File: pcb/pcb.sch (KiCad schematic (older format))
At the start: 21 parts

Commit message: 1n4148->1n4004 and connector changes
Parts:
- removed D? (x2): 1N4148, Diode_THT:D_DO-35_SOD27_P7.62mm_Horizontal, symbol Device:D_Small
- removed J?: Screw_Terminal_01x03, symbol Connector:Screw_Terminal_01x03
- added D? (x2): 1N4004, Diode_THT:D_DO-41_SOD81_P10.16mm_Horizontal, symbol Device:D_Small
- added J?: JST XH-3P, symbol Connector:Conn_01x03_Male
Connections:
- net +3V3: now also D?.2 (A)
- net GND: now also J?.3 (Pin_3)
- net UNLOCK_PIN: now also J?.2 (Pin_2)
- net VBUS: now also D?.1 (K), J?.1 (Pin_1)
- net at FH?.1: now also D?.2 (A)
- net at J?.1 (Pin_1), J?.2 (Pin_2), J?.3 (Pin_3)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: now also D?.1 (K)
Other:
- moved on the sheet: D?, FH?, J?
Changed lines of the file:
@@
 $EndComp
 $Comp
-L Connector:Screw_Terminal_01x03 J?
-U 1 1 6273A423
-P 8250 4700
-F 0 "J?" H 8168 4467 50  0000 C CNN
-F 1 "Screw_Terminal_01x03" H 8168 4466 50  0001 C CNN
-F 2 "" H 8250 4700 50  0001 C CNN
-F 3 "~" H 8250 4700 50  0001 C CNN
-	1    8250 4700
-	-1   0    0    1
-$EndComp
-$Comp
 L power:GND #PWR?
 U 1 1 6273AC33
@@
 L Connector:Screw_Terminal_01x02 J?
 U 1 1 627917BC
-P 8150 2900
-F 0 "J?" H 8230 2846 50  0000 L CNN
-F 1 "Screw_Terminal_01x02" H 8230 2801 50  0001 L CNN
-F 2 "" H 8150 2900 50  0001 C CNN
-F 3 "~" H 8150 2900 50  0001 C CNN
-	1    8150 2900
+P 8150 3000
+F 0 "J?" H 8230 2946 50  0000 L CNN
+F 1 "Screw_Terminal_01x02" H 8230 2901 50  0001 L CNN
+F 2 "" H 8150 3000 50  0001 C CNN
+F 3 "~" H 8150 3000 50  0001 C CNN
+	1    8150 3000
 	1    0    0    -1
 $EndComp
 Wire Wire Line
-	7900 3000 7950 3000
+	7900 3100 7950 3100
 Wire Wire Line
-	7900 2900 7950 2900
+	7900 3000 7950 3000
 $Comp
 L power:GND #PWR?
 U 1 1 627949F4
-P 7900 3200
-F 0 "#PWR?" H 7900 2950 50  0001 C CNN
-F 1 "GND" H 7905 3027 50  0000 C CNN
-F 2 "" H 7900 3200 50  0001 C CNN
-F 3 "" H 7900 3200 50  0001 C CNN
-	1    7900 3200
+P 7900 3300
+F 0 "#PWR?" H 7900 3050 50  0001 C CNN
+F 1 "GND" H 7905 3127 50  0000 C CNN
+F 2 "" H 7900 3300 50  0001 C CNN
+F 3 "" H 7900 3300 50  0001 C CNN
+	1    7900 3300
 	1    0    0    -1
 $EndComp
@@
 	8500 5000 8500 4800
 Wire Wire Line
-	7150 3150 7150 3200
+	7150 3250 7150 3300
 $Comp
 L Device:D_Zener_Small D?
 U 1 1 628663B7
-P 7150 3050
-F 0 "D?" V 7104 3118 50  0000 L CNN
-F 1 "Vz=15" V 7195 3118 50  0000 L CNN
-F 2 "" V 7150 3050 50  0001 C CNN
-F 3 "~" V 7150 3050 50  0001 C CNN
-	1    7150 3050
+P 7150 3150
+F 0 "D?" V 7104 3218 50  0000 L CNN
+F 1 "Vz=15" V 7195 3218 50  0000 L CNN
+F 2 "" V 7150 3150 50  0001 C CNN
+F 3 "~" V 7150 3150 50  0001 C CNN
+	1    7150 3150
 	0    -1   1    0
 $EndComp
@@
 L power:VBUS #PWR?
 U 1 1 62777264
-P 7150 2850
-F 0 "#PWR?" H 7150 2700 50  0001 C CNN
-F 1 "VBUS" H 7165 3023 50  0000 C CNN
-F 2 "" H 7150 2850 50  0001 C CNN
-F 3 "" H 7150 2850 50  0001 C CNN
-	1    7150 2850
+P 7150 2950
+F 0 "#PWR?" H 7150 2800 50  0001 C CNN
+F 1 "VBUS" H 7165 3123 50  0000 C CNN
+F 2 "" H 7150 2950 50  0001 C CNN
+F 3 "" H 7150 2950 50  0001 C CNN
+	1    7150 2950
 	1    0    0    -1
 $EndComp
@@
 L power:GND #PWR?
 U 1 1 628C5A12
-P 7150 3200
-F 0 "#PWR?" H 7150 2950 50  0001 C CNN
-F 1 "GND" H 7155 3027 50  0000 C CNN
-F 2 "" H 7150 3200 50  0001 C CNN
-F 3 "" H 7150 3200 50  0001 C CNN
-	1    7150 3200
+P 7150 3300
+F 0 "#PWR?" H 7150 3050 50  0001 C CNN
+F 1 "GND" H 7155 3127 50  0000 C CNN
+F 2 "" H 7150 3300 50  0001 C CNN
+F 3 "" H 7150 3300 50  0001 C CNN
+	1    7150 3300
 	1    0    0    -1
 $EndComp
 Wire Wire Line
-	7900 3000 7900 3200
+	7900 3100 7900 3300
 $Comp
 L power:+3V3 #PWR?
@@
 Text Label 7650 5950 3    50   ~ 0
 GPIO_0
-$Comp
-L Device:D_Small D?
-U 1 1 629C5C10
-P 7400 2900
-F 0 "D?" H 7400 3105 50  0000 C CNN
-F 1 "1N4148" H 7400 3014 50  0000 C CNN
-F 2 "Diode_THT:D_DO-35_SOD27_P7.62mm_Horizontal" H 7400 2725 50  0001 C CNN
-F 3 "https://assets.nexperia.com/documents/data-sheet/1N4148_1N4448.pdf" H 7400 2900 50  0001 C CNN
-	1    7400 2900
-	1    0    0    -1
-$EndComp
 Wire Wire Line
-	7500 2900 7700 2900
+	7500 3000 7700 3000
 $Comp
 L Device:Fuse_Small FH?
 U 1 1 628BC0F0
-P 7800 2900
-F 0 "FH?" H 7800 3085 50  0000 C CNN
-F 1 "F5196-ND" H 7800 2994 50  0000 C CNN
-F 2 "project:Blade Fuse Holder" H 7800 2900 50  0001 C CNN
-F 3 "https://www.digikey.com/en/products/detail/littelfuse-inc/178-6164-0002/2515918?s=N4IgTCBcDaIGIFYCMBOAbAWgHIBEQF0BfIA" H 7800 2900 50  0001 C CNN
-	1    7800 2900
+P 7800 3000
+F 0 "FH?" H 7800 3185 50  0000 C CNN
+F 1 "F5196-ND" H 7800 3094 50  0000 C CNN
+F 2 "project:Blade Fuse Holder" H 7800 3000 50  0001 C CNN
+F 3 "https://www.digikey.com/en/products/detail/littelfuse-inc/178-6164-0002/2515918?s=N4IgTCBcDaIGIFYCMBOAbAWgHIBEQF0BfIA" H 7800 3000 50  0001 C CNN
+	1    7800 3000
 	1    0    0    -1
 $EndComp
 Wire Wire Line
-	7150 2850 7150 2900
+	7150 2950 7150 3000
 Wire Wire Line
-	7300 2900 7150 2900
-Connection ~ 7150 2900
+	7300 3000 7150 3000
+Connection ~ 7150 3000
 Wire Wire Line
-	7150 2900 7150 2950
+	7150 3000 7150 3050
 Text Notes 6350 1550 0    50   ~ 10
 Power Input (5-15V)
@@
 Wire Wire Line
 	10100 1700 10100 1800
-$Comp
-L Device:D_Small D?
-U 1 1 629C1D64
-P 10100 1400
-F 0 "D?" V 10146 1332 50  0000 R CNN
-F 1 "1N4148" V 10055 1332 50  0000 R CNN
-F 2 "Diode_THT:D_DO-35_SOD27_P7.62mm_Horizontal" H 10100 1225 50  0001 C CNN
-F 3 "https://assets.nexperia.com/documents/data-sheet/1N4148_1N4448.pdf" H 10100 1400 50  0001 C CNN
-	1    10100 1400
-	0    -1   -1   0
-$EndComp
 Wire Wire Line
 	10100 1250 10100 1300
@@
 Wire Wire Line
 	950  6250 1550 6250
+$Comp
+L Device:D_Small D?
+U 1 1 6277C4DF
+P 7400 3000
+F 0 "D?" H 7400 3205 50  0000 C CNN
+F 1 "1N4004" H 7400 3114 50  0000 C CNN
+F 2 "Diode_THT:D_DO-41_SOD81_P10.16mm_Horizontal" H 7400 2825 50  0001 C CNN
+F 3 "http://www.vishay.com/docs/88503/1n4001.pdf" H 7400 3000 50  0001 C CNN
+	1    7400 3000
+	1    0    0    -1
+$EndComp
+$Comp
+L Connector:Conn_01x03_Male J?
+U 1 1 627915A3
+P 8250 4700
+F 0 "J?" H 8358 4981 50  0000 C CNN
+F 1 "JST XH-3P" H 8358 4890 50  0000 C CNN
+F 2 "" H 8250 4700 50  0001 C CNN
+F 3 "https://www.amazon.com/GeeBat-460pcs-Connector-Housing-Adapter/dp/B01MCZE2HM/" H 8250 4700 50  0001 C CNN
+	1    8250 4700
+	1    0    0    -1
+$EndComp
+$Comp
+L Device:D_Small D?
+U 1 1 627A484D
+P 10100 1400
+F 0 "D?" V 10146 1332 50  0000 R CNN
+F 1 "1N4004" V 10055 1332 50  0000 R CNN
+F 2 "Diode_THT:D_DO-41_SOD81_P10.16mm_Horizontal" H 10100 1225 50  0001 C CNN
+F 3 "http://www.vishay.com/docs/88503/1n4001.pdf" H 10100 1400 50  0001 C CNN
+	1    10100 1400
+	0    -1   -1   0
+$EndComp
 $EndSCHEMATC

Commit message: schematic pinout edits + documentation
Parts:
- added D?: Vz=3v3, symbol Device:D_Zener_Small
- added J?: JST XH-2P, symbol Connector:Conn_01x02_Male
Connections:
- net GND: now also D?.2 (A), J?.2 (Pin_2)
- net UNLOCK_LED: now reaches U?.11 (D4)
- net UNLOCK_LED: now also D?.1 (K), J?.1 (Pin_1)
- no-connect marks 3 -> 2
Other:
- note added: "Pins to Not Expose\n-------------------------\n- D3 is GPIO0 (used for programming)\n- RST connected to on-NodeMCU reset button (no need)\n- EN likely unused; connect to pin header just in case (special pin)\n- 10 (3V3) boxed in by D1,D2,D3 traces (no point)\n\nPinout\n-------------------------\n- D1 drives unlock relay\n- D4 is on-NodeMCU LED, double as external LED\n\nscrew terminal pins low sh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"
- note added: "door relay"
- note added: "layout: all pins and indicators must be\nclearly labelled on silkscreen"
- note added: "layout: all pins must be clearly labelled\non silkscreen"
- note added: "nfc comms"
- note added: "unlock led"
- note removed: "Pins to Not Expose\n-------------------------\n- D3 is GPIO0 (used for programming)\n- D4 is on-board LED for NodeMCU (already used)\n- RST connected to on-NodeMCU reset button (no need)\n- EN likely unused; connect to pin header just in case (special pin)\n- 10 (3V3) boxed in by D1,D2,D3 traces (no point)"
- note removed: "TODO\n- worth switching unlock to 3-pin keyed JST\n- dig up jst xh-4p for NFC"
- moved on the sheet: D?, J?, R?, U?

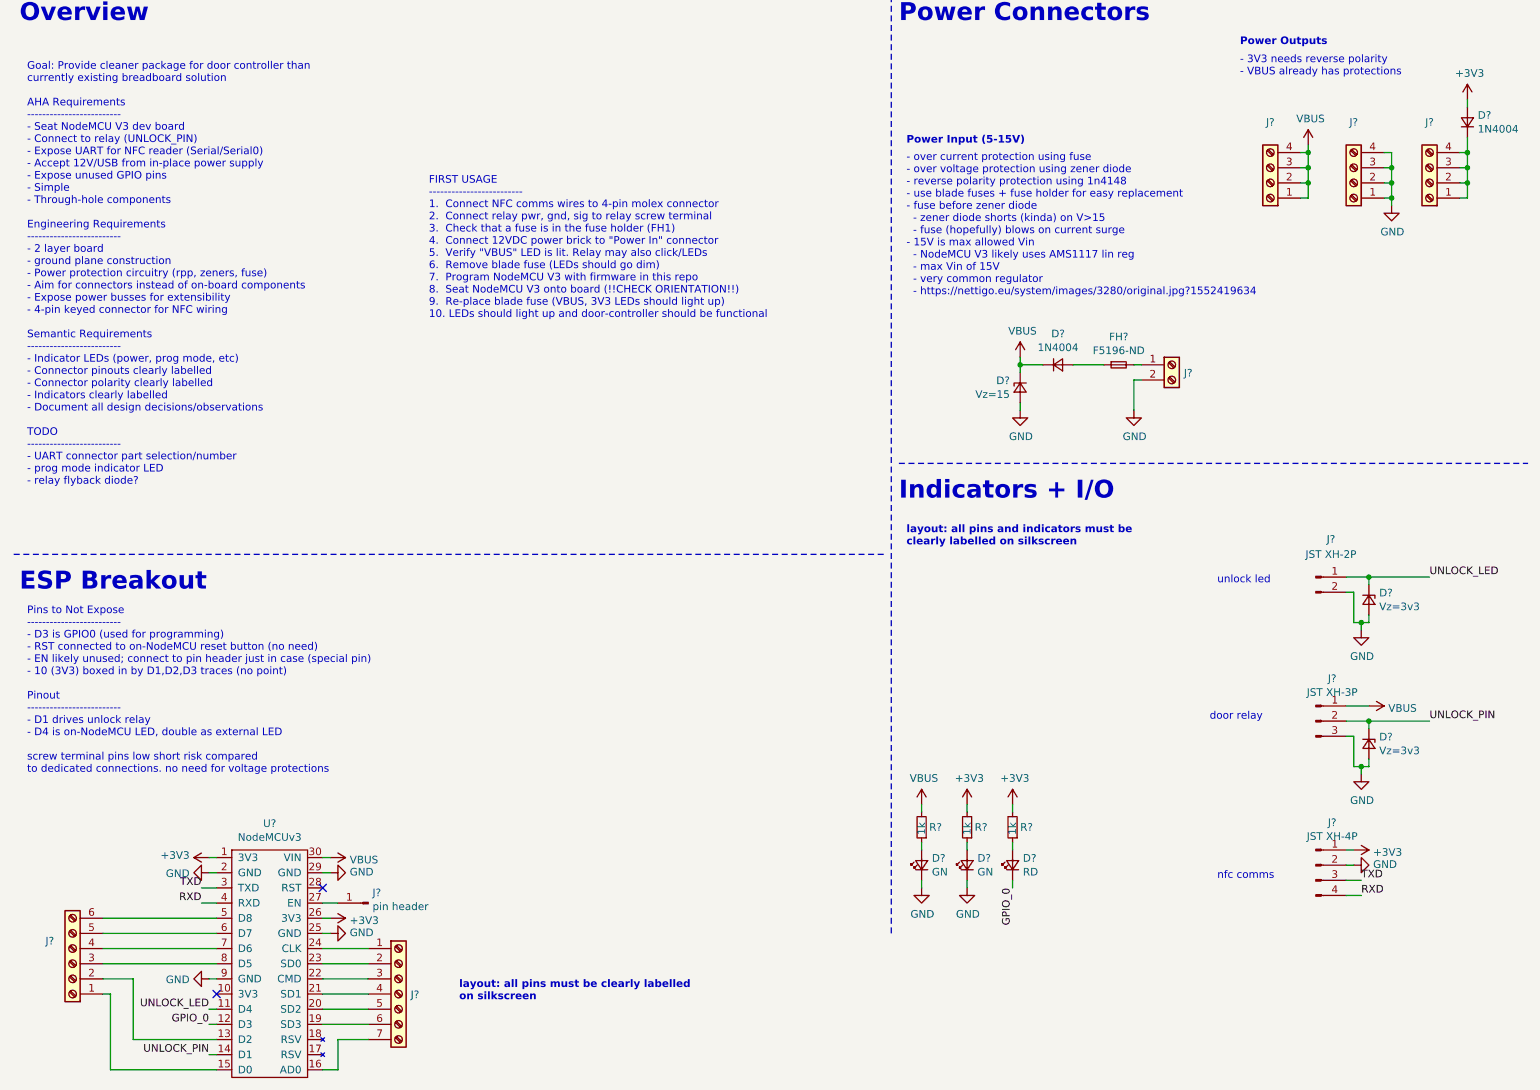
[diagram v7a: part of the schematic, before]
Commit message: ERC fixes - pwr_flags + nodemcuv3 power pins
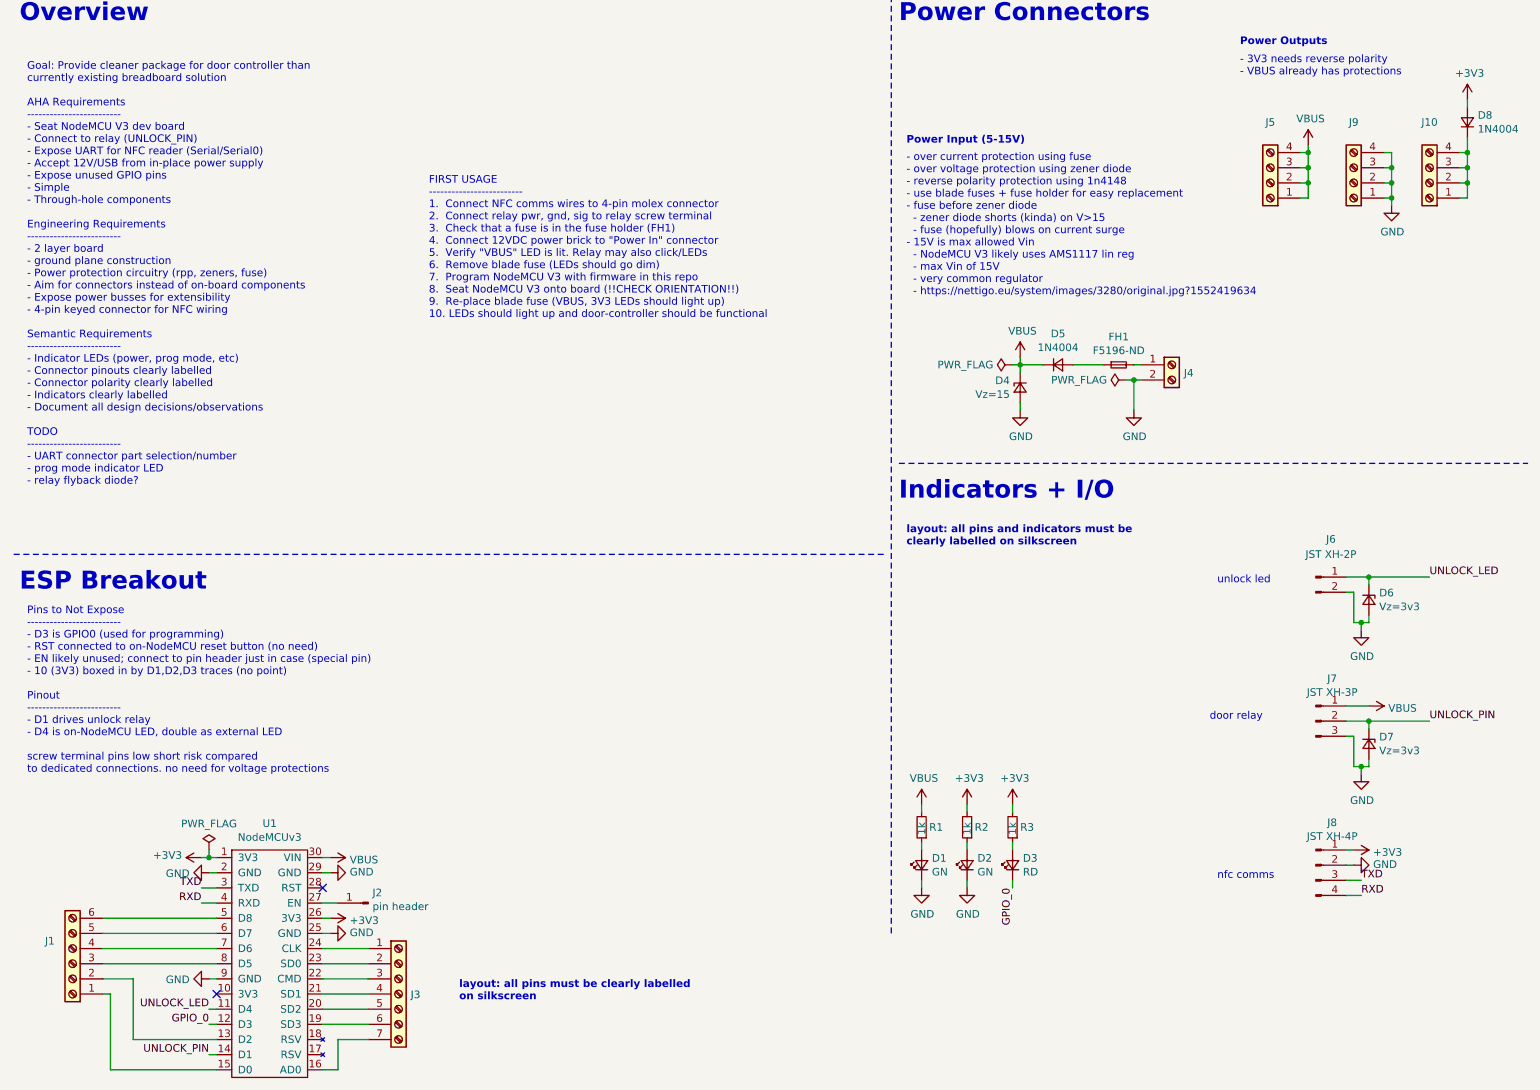
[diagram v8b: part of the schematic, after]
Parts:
- gave numbers to parts that had none: 23
